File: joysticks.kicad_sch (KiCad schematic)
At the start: 27 parts, among them J1 DB9_Male_MountingHoles, J2 DB9_Male_MountingHoles, J25 Joystick Ports Mezannine Lower, J26 Joystick Ports Mezannine Upper, SW1 Reset Button, U10 74LS06N, U11 74LS06N, U5 74LS06N, U6 74LVC374, U7 74LVC374, U8 74LS374, U9 74LS374

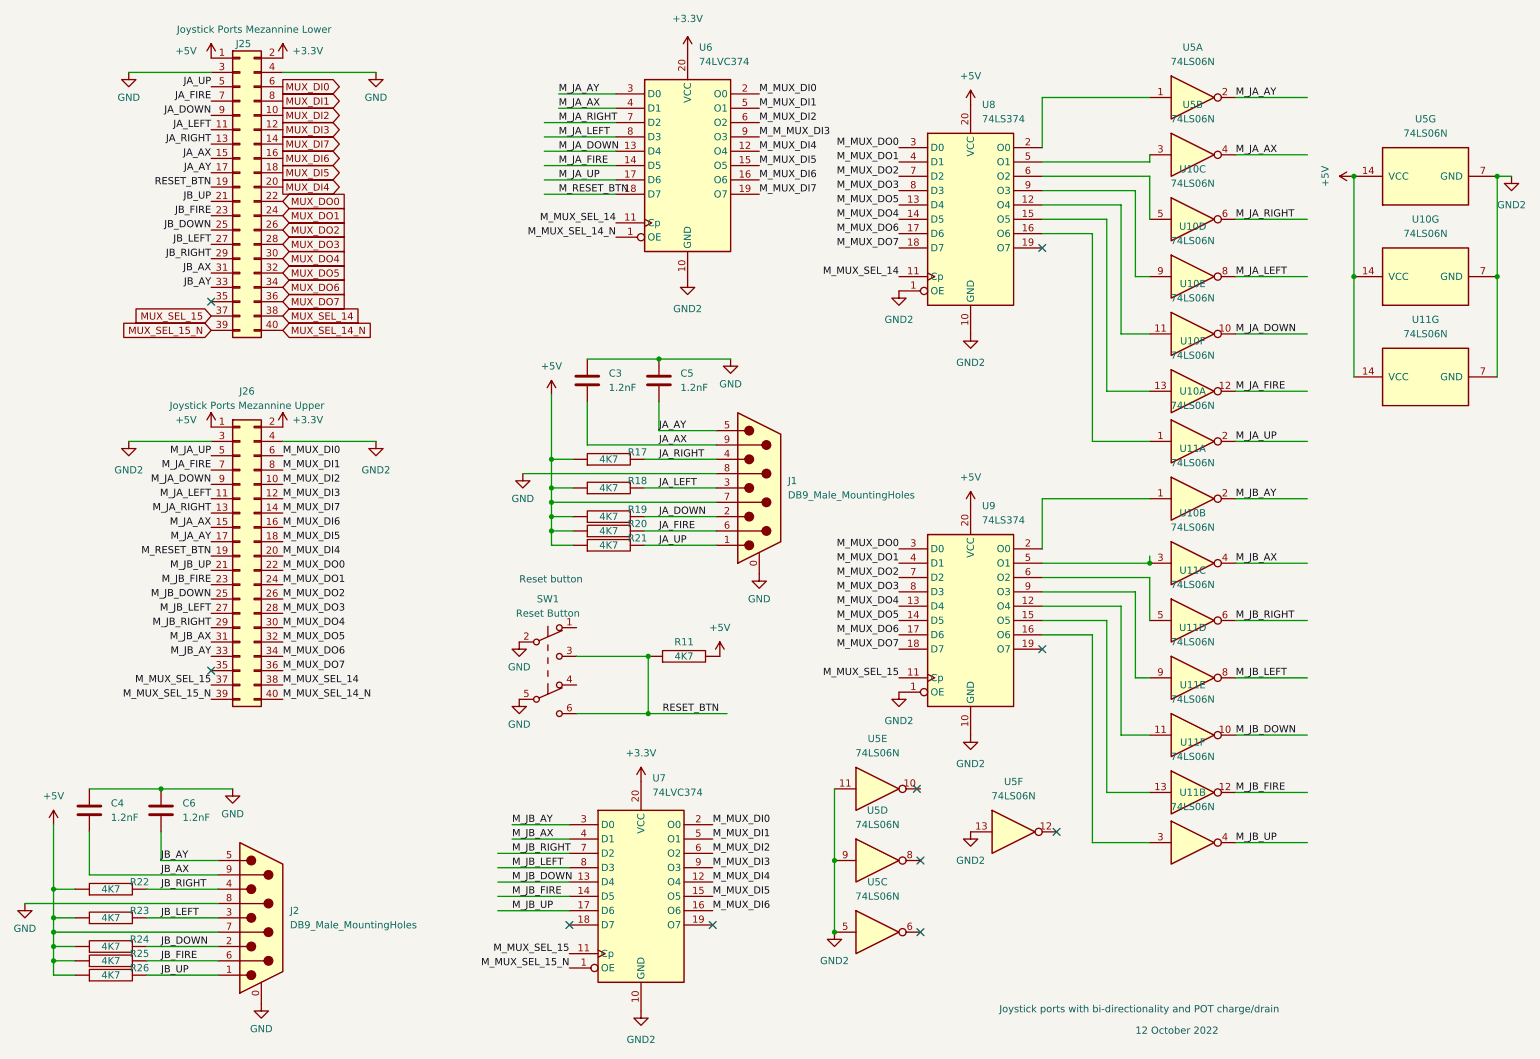
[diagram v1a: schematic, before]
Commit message: finish solving DRC violations
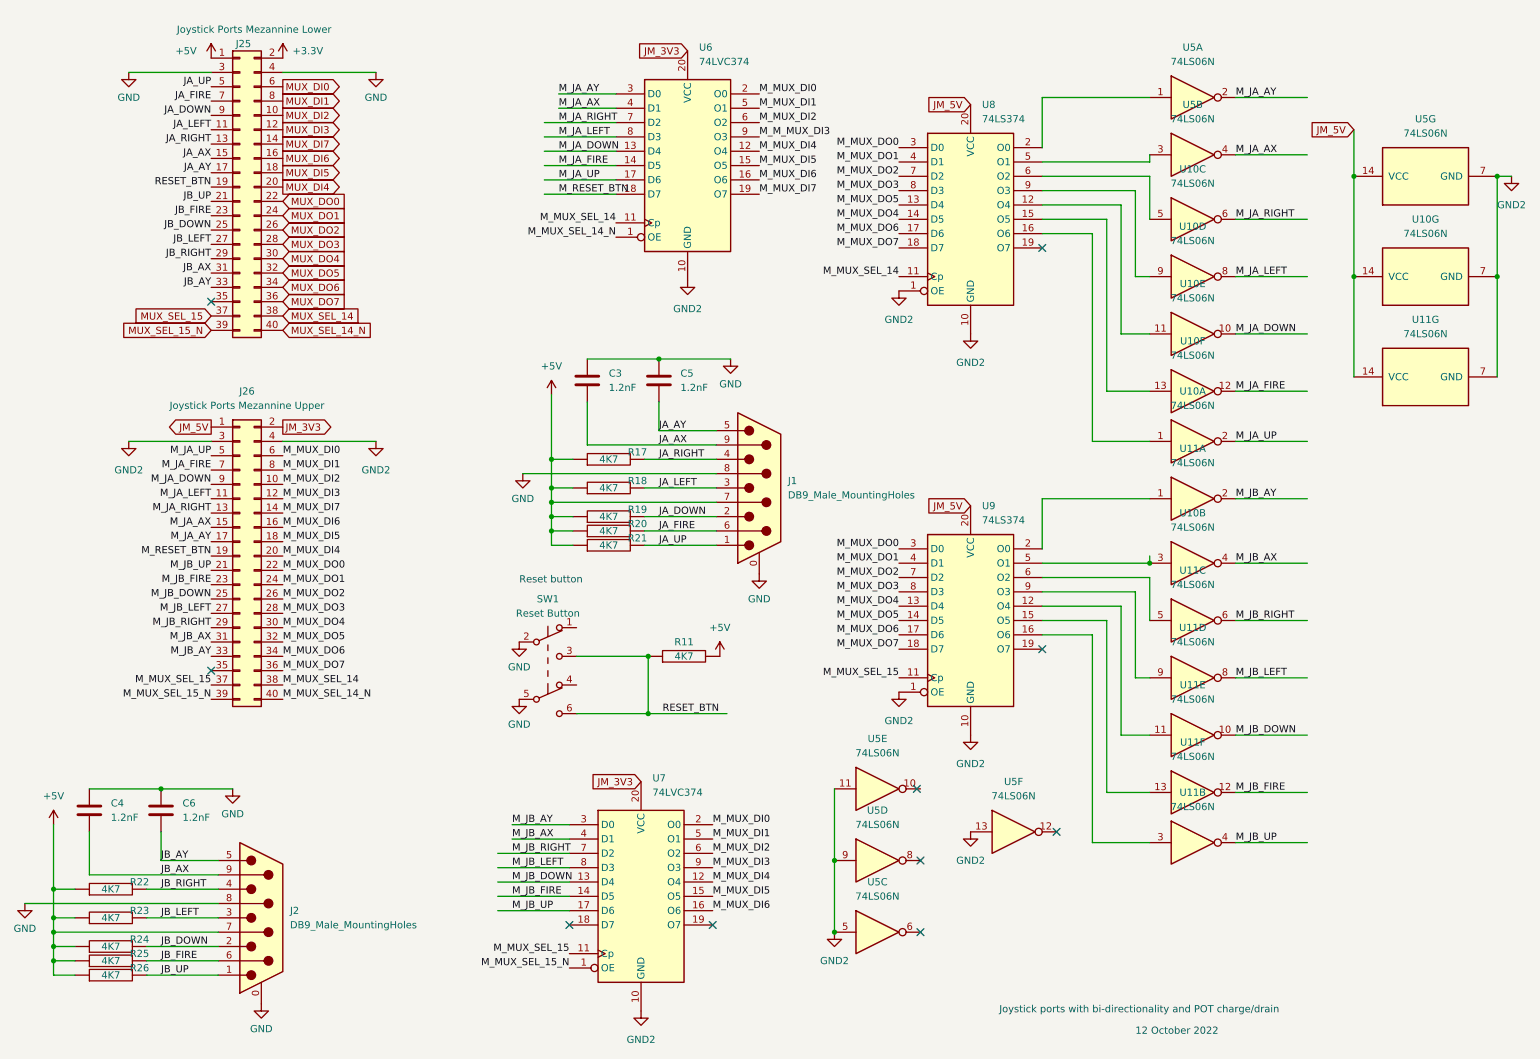
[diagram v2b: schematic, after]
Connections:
- net +3V3: no longer J26.2 (Pin_2), U6.20 (VCC), U7.20 (VCC)
- net +5V: no longer J26.1 (Pin_1), U10.14 (VCC), U11.14 (VCC), U5.14 (VCC), U8.20 (VCC), U9.20 (VCC)
- new net JM_3V3: J26.2 (Pin_2), U6.20 (VCC), U7.20 (VCC)
- new net JM_5V: J26.1 (Pin_1), U10.14 (VCC), U11.14 (VCC), U5.14 (VCC), U8.20 (VCC), U9.20 (VCC)
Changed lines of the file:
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@@
+    (stroke (width 0) (type default) (color 0 0 0 0))
+  )
+  (wire (pts (xy 252.095 33.655) (xy 252.095 41.91))
     (stroke (width 0) (type default) (color 0 0 0 0))
   )
@@
     )
   )
+  (global_label "JM_3V3" (shape input) (at 125.73 149.225 180) (fields_autoplaced)
+    (effects (font (size 1.27 1.27)) (justify right))
+    (property "Intersheet References" "${INTERSHEET_REFS}" (id 0) (at 116.4226 149.1456 0)
+      (effects (font (size 1.27 1.27)) (justify right) hide)
+    )
+  )
   (global_label "MUX_DI3" (shape output) (at 62.23 33.655 0) (fields_autoplaced)
     (effects (font (size 1.27 1.27)) (justify left))
@@
     )
   )
+  (global_label "JM_5V" (shape output) (at 49.53 86.36 180) (fields_autoplaced)
+    (effects (font (size 1.27 1.27)) (justify right))
+    (property "Intersheet References" "${INTERSHEET_REFS}" (id 0) (at 41.4321 86.2806 0)
+      (effects (font (size 1.27 1.27)) (justify right) hide)
+    )
+  )
   (global_label "MUX_DO4" (shape input) (at 62.23 56.515 0) (fields_autoplaced)
     (effects (font (size 1.27 1.27)) (justify left))
@@
     )
   )
+  (global_label "JM_5V" (shape input) (at 184.15 29.21 180) (fields_autoplaced)
+    (effects (font (size 1.27 1.27)) (justify right))
+    (property "Intersheet References" "${INTERSHEET_REFS}" (id 0) (at 176.0521 29.1306 0)
+      (effects (font (size 1.27 1.27)) (justify right) hide)
+    )
+  )
   (global_label "MUX_DO6" (shape input) (at 62.23 61.595 0) (fields_autoplaced)
     (effects (font (size 1.27 1.27)) (justify left))
@@
     )
   )
+  (global_label "JM_5V" (shape input) (at 184.15 100.33 180) (fields_autoplaced)
+    (effects (font (size 1.27 1.27)) (justify right))
+    (property "Intersheet References" "${INTERSHEET_REFS}" (id 0) (at 176.0521 100.2506 0)
+      (effects (font (size 1.27 1.27)) (justify right) hide)
+    )
+  )
   (global_label "MUX_DI7" (shape output) (at 62.23 36.195 0) (fields_autoplaced)
     (effects (font (size 1.27 1.27)) (justify left))
@@
     (property "Intersheet References" "${INTERSHEET_REFS}" (id 0) (at 73.4121 58.9756 0)
       (effects (font (size 1.27 1.27)) (justify left) hide)
+    )
+  )
+  (global_label "JM_5V" (shape input) (at 252.095 33.655 180) (fields_autoplaced)
+    (effects (font (size 1.27 1.27)) (justify right))
+    (property "Intersheet References" "${INTERSHEET_REFS}" (id 0) (at 243.9971 33.5756 0)
+      (effects (font (size 1.27 1.27)) (justify right) hide)
+    )
+  )
+  (global_label "JM_3V3" (shape output) (at 62.23 86.36 0) (fields_autoplaced)
+    (effects (font (size 1.27 1.27)) (justify left))
+    (property "Intersheet References" "${INTERSHEET_REFS}" (id 0) (at 71.5374 86.2806 0)
+      (effects (font (size 1.27 1.27)) (justify left) hide)
+    )
+  )
+  (global_label "JM_3V3" (shape input) (at 133.985 19.685 180) (fields_autoplaced)
+    (effects (font (size 1.27 1.27)) (justify right))
+    (property "Intersheet References" "${INTERSHEET_REFS}" (id 0) (at 124.6776 19.6056 0)
+      (effects (font (size 1.27 1.27)) (justify right) hide)
     )
   )
@@
     (pin "12")
     (pin "13")
-  )
-  (symbol (lib_id "power:+5V") (at 49.53 86.36 0) (unit 1)
-    (in_bom yes) (on_board yes)
-    (property "Reference" "#PWR0130" (id 0) (at 49.53 90.17 0)
-      (effects (font (size 1.27 1.27)) hide)
-    )
-    (property "Value" "+5V" (id 1) (at 45.085 85.09 0))
-    (property "Footprint" "" (id 2) (at 49.53 86.36 0)
-      (effects (font (size 1.27 1.27)) hide)
-    )
-    (property "Datasheet" "" (id 3) (at 49.53 86.36 0)
-      (effects (font (size 1.27 1.27)) hide)
-    )
-    (pin "1")
   )
   (symbol (lib_id "Connector_Generic:Conn_02x20_Odd_Even") (at 54.61 109.22 0) (unit 1)
@@
     (pin "2")
   )
-  (symbol (lib_id "power:+5V") (at 252.095 41.91 90) (unit 1)
-    (in_bom yes) (on_board yes) (fields_autoplaced)
-    (property "Reference" "#PWR0133" (id 0) (at 255.905 41.91 0)
-      (effects (font (size 1.27 1.27)) hide)
-    )
-    (property "Value" "+5V" (id 1) (at 247.015 41.91 0))
-    (property "Footprint" "" (id 2) (at 252.095 41.91 0)
-      (effects (font (size 1.27 1.27)) hide)
-    )
-    (property "Datasheet" "" (id 3) (at 252.095 41.91 0)
-      (effects (font (size 1.27 1.27)) hide)
-    )
-    (pin "1")
-  )
   (symbol (lib_id "pspice:R") (at 120.015 92.075 90) (unit 1)
     (in_bom yes) (on_board yes)
@@
     (pin "2")
   )
-  (symbol (lib_id "power:+3.3V") (at 125.73 149.225 0) (unit 1)
-    (in_bom yes) (on_board yes) (fields_autoplaced)
-    (property "Reference" "#PWR0126" (id 0) (at 125.73 153.035 0)
-      (effects (font (size 1.27 1.27)) hide)
-    )
-    (property "Value" "+3.3V" (id 1) (at 125.73 144.145 0))
-    (property "Footprint" "" (id 2) (at 125.73 149.225 0)
-      (effects (font (size 1.27 1.27)) hide)
-    )
-    (property "Datasheet" "" (id 3) (at 125.73 149.225 0)
-      (effects (font (size 1.27 1.27)) hide)
-    )
-    (pin "1")
-  )
-  (symbol (lib_id "power:+3.3V") (at 133.985 19.685 0) (unit 1)
-    (in_bom yes) (on_board yes) (fields_autoplaced)
-    (property "Reference" "#PWR0128" (id 0) (at 133.985 23.495 0)
-      (effects (font (size 1.27 1.27)) hide)
-    )
-    (property "Value" "+3.3V" (id 1) (at 133.985 13.97 0))
-    (property "Footprint" "" (id 2) (at 133.985 19.685 0)
-      (effects (font (size 1.27 1.27)) hide)
-    )
-    (property "Datasheet" "" (id 3) (at 133.985 19.685 0)
-      (effects (font (size 1.27 1.27)) hide)
-    )
-    (pin "1")
-  )
   (symbol (lib_id "pspice:R") (at 31.75 183.515 90) (unit 1)
     (in_bom yes) (on_board yes)
@@
     (pin "2")
   )
-  (symbol (lib_id "power:+3.3V") (at 62.23 86.36 0) (unit 1)
-    (in_bom yes) (on_board yes)
-    (property "Reference" "#PWR0129" (id 0) (at 62.23 90.17 0)
-      (effects (font (size 1.27 1.27)) hide)
-    )
-    (property "Value" "+3.3V" (id 1) (at 66.675 85.09 0))
-    (property "Footprint" "" (id 2) (at 62.23 86.36 0)
-      (effects (font (size 1.27 1.27)) hide)
-    )
-    (property "Datasheet" "" (id 3) (at 62.23 86.36 0)
-      (effects (font (size 1.27 1.27)) hide)
-    )
-    (pin "1")
-  )
   (symbol (lib_id "74xx:74LS06N") (at 264.795 77.47 90) (unit 7)
     (in_bom yes) (on_board yes) (fields_autoplaced)
@@
     (pin "1")
     (pin "2")
-  )
-  (symbol (lib_id "power:+5V") (at 184.15 100.33 0) (unit 1)
-    (in_bom yes) (on_board yes) (fields_autoplaced)
-    (property "Reference" "#PWR0147" (id 0) (at 184.15 104.14 0)
-      (effects (font (size 1.27 1.27)) hide)
-    )
-    (property "Value" "+5V" (id 1) (at 184.15 95.25 0))
-    (property "Footprint" "" (id 2) (at 184.15 100.33 0)
-      (effects (font (size 1.27 1.27)) hide)
-    )
-    (property "Datasheet" "" (id 3) (at 184.15 100.33 0)
-      (effects (font (size 1.27 1.27)) hide)
-    )
-    (pin "1")
   )
   (symbol (lib_id "power:GND2") (at 184.15 69.85 0) (unit 1)
@@
     (pin "2")
   )
-  (symbol (lib_id "power:+5V") (at 184.15 29.21 0) (unit 1)
-    (in_bom yes) (on_board yes) (fields_autoplaced)
-    (property "Reference" "#PWR0151" (id 0) (at 184.15 33.02 0)
-      (effects (font (size 1.27 1.27)) hide)
-    )
-    (property "Value" "+5V" (id 1) (at 184.15 24.13 0))
-    (property "Footprint" "" (id 2) (at 184.15 29.21 0)
-      (effects (font (size 1.27 1.27)) hide)
-    )
-    (property "Datasheet" "" (id 3) (at 184.15 29.21 0)
-      (effects (font (size 1.27 1.27)) hide)
-    )
-    (pin "1")
-  )
   (symbol (lib_id "pspice:R") (at 31.75 180.975 90) (unit 1)
